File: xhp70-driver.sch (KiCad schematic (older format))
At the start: 13 parts

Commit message: Layout schematic, created AL8871Q symbol and footprint. Layout PCB.
Pending values for components and PCB traces.
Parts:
- C1, C2, C3: renamed from C?; footprint (none) -> Capacitor_SMD:C_1206_3216Metric_Pad1.33x1.80mm_HandSolder
- D1: renamed from D?; footprint (none) -> Diode_SMD:D_PowerDI-5
- D2: renamed from D?; footprint (none) -> Connector_Molex:Molex_Sabre_46007-1102_1x02_P7.49mm_Horizontal
- L1: renamed from L?; footprint (none) -> Inductor_SMD:L_12x12mm_H8mm
- Q1: renamed from Q?; footprint (none) -> Package_TO_SOT_SMD:TO-252-2
- R1, R2, R3, R4, R5: renamed from R?; footprint (none) -> Resistor_SMD:R_1206_3216Metric_Pad1.30x1.75mm_HandSolder
- U1: renamed from U?; footprint (none) -> xhp70-driver:AL8871Q
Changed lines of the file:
@@
 $EndDescr
 $Comp
-L LED-driver:AL8871Q U?
+L LED-driver:AL8871Q U1
 U 1 1 6031458B
 P 5300 3400
-F 0 "U?" H 6094 3471 50  0000 L CNN
+F 0 "U1" H 6094 3471 50  0000 L CNN
 F 1 "AL8871Q" H 6094 3380 50  0000 L CNN
-F 2 "" H 5250 4650 50  0001 C CNN
+F 2 "xhp70-driver:AL8871Q" H 5250 4650 50  0001 C CNN
 F 3 "" H 5250 4650 50  0001 C CNN
 	1    5300 3400
@@
 $EndComp
 $Comp
-L power:+BATT #PWR?
+L power:+BATT #PWR0101
 U 1 1 60315055
 P 2450 2200
-F 0 "#PWR?" H 2450 2050 50  0001 C CNN
+F 0 "#PWR0101" H 2450 2050 50  0001 C CNN
 F 1 "+BATT" H 2465 2373 50  0000 C CNN
 F 2 "" H 2450 2200 50  0001 C CNN
@@
 $EndComp
 $Comp
-L power:GND #PWR?
+L power:GND #PWR0102
 U 1 1 603158B1
 P 5500 5050
-F 0 "#PWR?" H 5500 4800 50  0001 C CNN
+F 0 "#PWR0102" H 5500 4800 50  0001 C CNN
 F 1 "GND" H 5505 4877 50  0000 C CNN
 F 2 "" H 5500 5050 50  0001 C CNN
@@
 $EndComp
 $Comp
-L Device:R R?
+L Device:R R1
 U 1 1 60317199
 P 2800 3950
-F 0 "R?" H 2870 3996 50  0000 L CNN
+F 0 "R1" H 2870 3996 50  0000 L CNN
 F 1 "R" H 2870 3905 50  0000 L CNN
-F 2 "" V 2730 3950 50  0001 C CNN
+F 2 "Resistor_SMD:R_1206_3216Metric_Pad1.30x1.75mm_HandSolder" V 2730 3950 50  0001 C CNN
 F 3 "~" H 2800 3950 50  0001 C CNN
 	1    2800 3950
@@
 $EndComp
 $Comp
-L Device:C C?
+L Device:C C1
 U 1 1 60318EA7
 P 2450 3100
-F 0 "C?" H 2565 3146 50  0000 L CNN
+F 0 "C1" H 2565 3146 50  0000 L CNN
 F 1 "C" H 2565 3055 50  0000 L CNN
-F 2 "" H 2488 2950 50  0001 C CNN
+F 2 "Capacitor_SMD:C_1206_3216Metric_Pad1.33x1.80mm_HandSolder" H 2488 2950 50  0001 C CNN
 F 3 "~" H 2450 3100 50  0001 C CNN
 	1    2450 3100
@@
 $EndComp
 $Comp
-L Device:R R?
+L Device:R R3
 U 1 1 6031A435
 P 3400 3950
-F 0 "R?" H 3470 3996 50  0000 L CNN
+F 0 "R3" H 3470 3996 50  0000 L CNN
 F 1 "R" H 3470 3905 50  0000 L CNN
-F 2 "" V 3330 3950 50  0001 C CNN
+F 2 "Resistor_SMD:R_1206_3216Metric_Pad1.30x1.75mm_HandSolder" V 3330 3950 50  0001 C CNN
 F 3 "~" H 3400 3950 50  0001 C CNN
 	1    3400 3950
@@
 $EndComp
 $Comp
-L Device:R R?
+L Device:R R4
 U 1 1 6031AA09
 P 3400 4500
-F 0 "R?" H 3470 4546 50  0000 L CNN
+F 0 "R4" H 3470 4546 50  0000 L CNN
 F 1 "R" H 3470 4455 50  0000 L CNN
-F 2 "" V 3330 4500 50  0001 C CNN
+F 2 "Resistor_SMD:R_1206_3216Metric_Pad1.30x1.75mm_HandSolder" V 3330 4500 50  0001 C CNN
 F 3 "~" H 3400 4500 50  0001 C CNN
 	1    3400 4500
@@
 $EndComp
 $Comp
-L Device:R R?
+L Device:R R2
 U 1 1 6031AE07
 P 2800 4500
-F 0 "R?" H 2870 4546 50  0000 L CNN
+F 0 "R2" H 2870 4546 50  0000 L CNN
 F 1 "R" H 2870 4455 50  0000 L CNN
-F 2 "" V 2730 4500 50  0001 C CNN
+F 2 "Resistor_SMD:R_1206_3216Metric_Pad1.30x1.75mm_HandSolder" V 2730 4500 50  0001 C CNN
 F 3 "~" H 2800 4500 50  0001 C CNN
 	1    2800 4500
@@
 $EndComp
 $Comp
-L Device:C C?
+L Device:C C2
 U 1 1 6031B075
 P 4350 4500
-F 0 "C?" H 4465 4546 50  0000 L CNN
+F 0 "C2" H 4465 4546 50  0000 L CNN
 F 1 "C" H 4465 4455 50  0000 L CNN
-F 2 "" H 4388 4350 50  0001 C CNN
+F 2 "Capacitor_SMD:C_1206_3216Metric_Pad1.33x1.80mm_HandSolder" H 4388 4350 50  0001 C CNN
 F 3 "~" H 4350 4500 50  0001 C CNN
 	1    4350 4500
@@
 $EndComp
 $Comp
-L Device:R R?
+L Device:R R5
 U 1 1 6031BBB3
 P 5500 2200
-F 0 "R?" V 5293 2200 50  0000 C CNN
+F 0 "R5" V 5293 2200 50  0000 C CNN
 F 1 "R" V 5384 2200 50  0000 C CNN
-F 2 "" V 5430 2200 50  0001 C CNN
+F 2 "Resistor_SMD:R_1206_3216Metric_Pad1.30x1.75mm_HandSolder" V 5430 2200 50  0001 C CNN
 F 3 "~" H 5500 2200 50  0001 C CNN
 	1    5500 2200
@@
 $EndComp
 $Comp
-L pspice:INDUCTOR L?
+L pspice:INDUCTOR L1
 U 1 1 6031C7F1
 P 7850 2750
-F 0 "L?" V 7804 2828 50  0000 L CNN
+F 0 "L1" V 7804 2828 50  0000 L CNN
 F 1 "INDUCTOR" V 7895 2828 50  0000 L CNN
-F 2 "" H 7850 2750 50  0001 C CNN
+F 2 "Inductor_SMD:L_12x12mm_H8mm" H 7850 2750 50  0001 C CNN
 F 3 "~" H 7850 2750 50  0001 C CNN
 	1    7850 2750
@@
 $EndComp
 $Comp
-L Device:Q_NMOS_GDS Q?
+L Device:Q_NMOS_GDS Q1
 U 1 1 603205DA
 P 7750 3350
-F 0 "Q?" H 7954 3396 50  0000 L CNN
+F 0 "Q1" H 7954 3396 50  0000 L CNN
 F 1 "Q_NMOS_GDS" H 7954 3305 50  0000 L CNN
-F 2 "" H 7950 3450 50  0001 C CNN
+F 2 "Package_TO_SOT_SMD:TO-252-2" H 7950 3450 50  0001 C CNN
 F 3 "~" H 7750 3350 50  0001 C CNN
 	1    7750 3350
@@
 $EndComp
 $Comp
-L Device:D D?
+L Device:D D1
 U 1 1 603221B3
 P 8700 3000
-F 0 "D?" H 8700 2783 50  0000 C CNN
+F 0 "D1" H 8700 2783 50  0000 C CNN
 F 1 "D" H 8700 2874 50  0000 C CNN
-F 2 "" H 8700 3000 50  0001 C CNN
+F 2 "Diode_SMD:D_PowerDI-5" H 8700 3000 50  0001 C CNN
 F 3 "~" H 8700 3000 50  0001 C CNN
 	1    8700 3000
@@
 $EndComp
 $Comp
-L Device:C C?
+L Device:C C3
 U 1 1 60322E55
 P 9000 2350
-F 0 "C?" H 9115 2396 50  0000 L CNN
+F 0 "C3" H 9115 2396 50  0000 L CNN
 F 1 "C" H 9115 2305 50  0000 L CNN
-F 2 "" H 9038 2200 50  0001 C CNN
+F 2 "Capacitor_SMD:C_1206_3216Metric_Pad1.33x1.80mm_HandSolder" H 9038 2200 50  0001 C CNN
 F 3 "~" H 9000 2350 50  0001 C CNN
 	1    9000 2350
@@
 $EndComp
 $Comp
-L Device:LED D?
+L Device:LED D2
 U 1 1 60323B1E
 P 9750 2350
-F 0 "D?" V 9697 2430 50  0000 L CNN
+F 0 "D2" V 9697 2430 50  0000 L CNN
 F 1 "LED" V 9788 2430 50  0000 L CNN
-F 2 "" H 9750 2350 50  0001 C CNN
+F 2 "Connector_Molex:Molex_Sabre_46007-1102_1x02_P7.49mm_Horizontal" H 9750 2350 50  0001 C CNN
 F 3 "~" H 9750 2350 50  0001 C CNN
 	1    9750 2350

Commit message: Added Attiny85 MCU to control PWM of AL8871Q
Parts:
- added H1, H2, H3, H4, H5: MountingHole, MountingHole:MountingHole_2.2mm_M2_ISO7380_Pad, symbol Mechanical:MountingHole
- added J1: LEMO2, xhp70-driver:TestPoint_2Pad_4.0x4.0mm, symbol Connector:LEMO2
- added J2: AVR-ISP-6, Connector_JST:JST_SH_BM06B-SRSS-TB_1x06-1MP_P1.00mm_Vertical, symbol Connector:AVR-ISP-6
- added J3: Conn_01x02_Male, Connector_JST:JST_SH_BM02B-SRSS-TB_1x02-1MP_P1.00mm_Vertical, symbol Connector:Conn_01x02_Male
- added TH1: 10K, xhp70-driver:TestPoint_2Pad_4.0x4.0mm, symbol Device:Thermistor_NTC
- added U2: ATtiny85-20SU, Package_SO:SOIJ-8_5.3x5.3mm_P1.27mm, symbol MCU_Microchip_ATtiny:ATtiny85-20SU
- added U3: L7805, Package_TO_SOT_SMD:SOT-23, symbol Regulator_Linear:L7805
- D2: footprint Connector_Molex:Molex_Sabre_46007-1102_1x02_P7.49mm_Horizontal -> xhp70-driver:TestPoint_2Pad_4.0x4.0mm
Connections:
- net labels added: Batt+, PWM
- wire segments 59 -> 93
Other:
- moved on the sheet: C1, C2, C3, D2, L1, Q1, R1, R2, R3, R5, U1

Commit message: Added components and route connections in xhp70-driver-test-route.pro file
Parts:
- removed D1: D, Diode_SMD:D_PowerDI-5, symbol Device:D
- removed R5: R, Resistor_SMD:R_1206_3216Metric_Pad1.30x1.75mm_HandSolder, symbol Device:R
- added C4: 1uF, Capacitor_SMD:C_1206_3216Metric_Pad1.33x1.80mm_HandSolder, symbol Device:C
- added C5: 100nF, Capacitor_SMD:C_0805_2012Metric, symbol Device:C
- added C6: 330pF, Capacitor_SMD:C_0805_2012Metric, symbol Device:C
- added D1: D_Schottky, xhp70-driver:TO-220-2_Horizontal_TabUp-no-mounting-hole, symbol Device:D_Schottky
- C1, C2: value C -> 10uF; Field4 (none) -> X7R, 100V
- C3: value C -> 1uF; Field4 (none) -> X7R, 100V, 1206
- J2: footprint Connector_JST:JST_SH_BM06B-SRSS-TB_1x06-1MP_P1.00mm_Vertical -> Connector_PinHeader_1.00mm:PinHeader_1x06_P1.00mm_Vertical
- Q1: footprint Package_TO_SOT_SMD:TO-252-2 -> xhp70-driver:TO-220-3_Horizontal_TabUp-no-mounting-hole
- R1: value R -> 0.09; footprint Resistor_SMD:R_1206_3216Metric_Pad1.30x1.75mm_HandSolder -> Resistor_SMD:R_2512_6332Metric; Field4 (none) -> 1W
- R2: value R -> 0.082; footprint Resistor_SMD:R_1206_3216Metric_Pad1.30x1.75mm_HandSolder -> Resistor_SMD:R_2512_6332Metric; Field4 (none) -> 1W
- R3: value R -> 2.2K; footprint Resistor_SMD:R_1206_3216Metric_Pad1.30x1.75mm_HandSolder -> Resistor_SMD:R_0805_2012Metric
- R4: value R -> 1.3K; footprint Resistor_SMD:R_1206_3216Metric_Pad1.30x1.75mm_HandSolder -> Resistor_SMD:R_0805_2012Metric
- R5: renamed from TH1; footprint xhp70-driver:TestPoint_2Pad_4.0x4.0mm -> Connector_JST:JST_SH_BM02B-SRSS-TB_1x02-1MP_P1.00mm_Vertical
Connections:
- wire segments 93 -> 92
- no-connect marks 2 -> 4
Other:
- moved on the sheet: C1, C3, D2, H1, H2, H4, H5, L1, Q1, R1, R2, R3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

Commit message: Reposition and changed connector. Reroute traces
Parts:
- J2: footprint Connector_PinHeader_1.00mm:PinHeader_1x06_P1.00mm_Vertical -> Connector_JST:JST_SH_BM06B-SRSS-TB_1x06-1MP_P1.00mm_Vertical
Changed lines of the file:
@@
 F 0 "J2" H 5370 6596 50  0000 R CNN
 F 1 "AVR-ISP-6" H 5370 6505 50  0000 R CNN
-F 2 "Connector_PinHeader_1.00mm:PinHeader_1x06_P1.00mm_Vertical" V 5450 6550 50  0001 C CNN
+F 2 "Connector_JST:JST_SH_BM06B-SRSS-TB_1x06-1MP_P1.00mm_Vertical" V 5450 6550 50  0001 C CNN
 F 3 " ~" H 4425 5950 50  0001 C CNN
 	1    5700 6500

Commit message: Updates
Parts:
- removed J3: Conn_01x02_Male, Connector_JST:JST_SH_BM02B-SRSS-TB_1x02-1MP_P1.00mm_Vertical, symbol Connector:Conn_01x02_Male
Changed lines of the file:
@@
 	4100 6450 4100 6550
-Wire Wire Line
-	4100 6550 4550 6550
-$Comp
-L Connector:Conn_01x02_Male J3
-U 1 1 603B34ED
-P 5200 7500
-F 0 "J3" H 5172 7382 50  0000 R CNN
-F 1 "Conn_01x02_Male" H 5172 7473 50  0000 R CNN
-F 2 "Connector_JST:JST_SH_BM02B-SRSS-TB_1x02-1MP_P1.00mm_Vertical" H 5200 7500 50  0001 C CNN
-F 3 "~" H 5200 7500 50  0001 C CNN
-	1    5200 7500
-	-1   0    0    1
-$EndComp
-Wire Wire Line
-	5000 7500 2150 7500
-Wire Wire Line
-	2150 7500 2150 5650
-Wire Wire Line
-	2100 5650 2150 5650
-Connection ~ 2150 5650
-Wire Wire Line
-	2150 5650 3250 5650
-Wire Wire Line
-	4550 6550 4550 7400
-Wire Wire Line
-	4550 7400 5000 7400
 Wire Wire Line
 	4300 6300 4300 6350
@@
 Wire Wire Line
 	5150 6500 5300 6500
-Connection ~ 4550 6550
-Wire Wire Line
-	4550 6550 5150 6550
 Wire Wire Line
 	4850 6250 4850 6400
@@
 Wire Wire Line
 	3450 1850 3900 1850
+Wire Wire Line
+	4100 6550 5150 6550
+Wire Wire Line
+	2100 5650 3250 5650
 $EndSCHEMATC

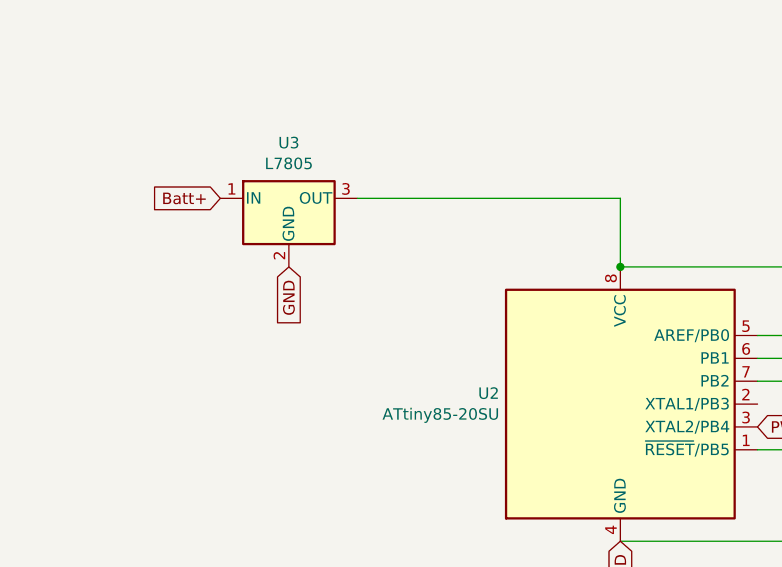
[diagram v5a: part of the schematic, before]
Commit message: LED driver rev.1b - Added decoupling Capacitors for Attiny
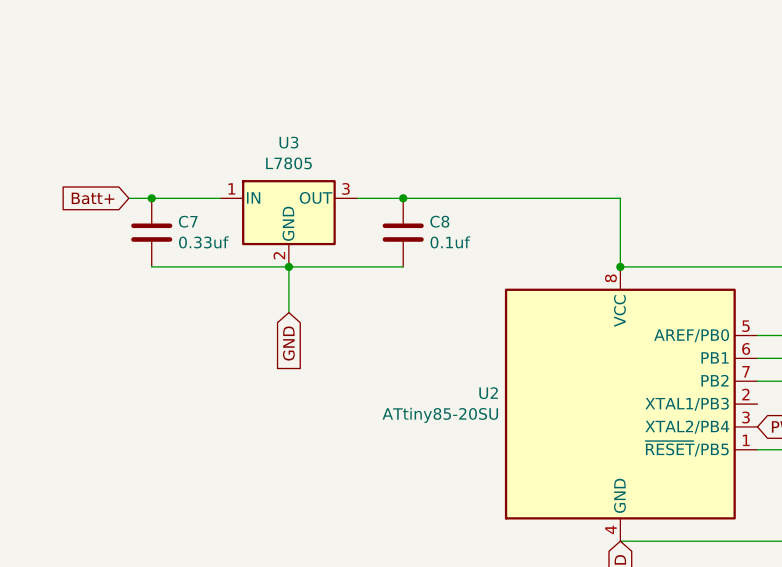
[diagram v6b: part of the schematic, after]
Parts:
- added C7: 0.33uf, Capacitor_SMD:C_0805_2012Metric, symbol Device:C
- added C8: 0.1uf, Capacitor_SMD:C_0805_2012Metric, symbol Device:C
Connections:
- net +BATT: now also C7.1
- net GND: now also C7.2, C8.2
- net at J2.2 (VCC), U2.8 (VCC), U3.3 (OUT): now also C8.1
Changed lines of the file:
@@
 Text GLabel 3850 6650 2    50   Input ~ 0
 PWM
-Text GLabel 1800 5950 3    50   Input ~ 0
+Text GLabel 1800 6150 3    50   Input ~ 0
 GND
 Text GLabel 3250 7150 3    50   Input ~ 0
 GND
-Text GLabel 1500 5650 0    50   Input ~ 0
+Text GLabel 1100 5650 0    50   Input ~ 0
 Batt+
 Wire Wire Line
@@
 	4100 6550 5150 6550
 Wire Wire Line
-	2100 5650 3250 5650
+	2100 5650 2300 5650
+$Comp
+L Device:C C7
+U 1 1 6043B427
+P 1200 5800
+F 0 "C7" H 1315 5846 50  0000 L CNN
+F 1 "0.33uf" H 1315 5755 50  0000 L CNN
+F 2 "Capacitor_SMD:C_0805_2012Metric" H 1238 5650 50  0001 C CNN
+F 3 "~" H 1200 5800 50  0001 C CNN
+	1    1200 5800
+	1    0    0    -1
+$EndComp
+$Comp
+L Device:C C8
+U 1 1 6043C0F6
+P 2300 5800
+F 0 "C8" H 2415 5846 50  0000 L CNN
+F 1 "0.1uf" H 2415 5755 50  0000 L CNN
+F 2 "Capacitor_SMD:C_0805_2012Metric" H 2338 5650 50  0001 C CNN
+F 3 "~" H 2300 5800 50  0001 C CNN
+	1    2300 5800
+	1    0    0    -1
+$EndComp
+Connection ~ 2300 5650
+Wire Wire Line
+	2300 5650 3250 5650
+Wire Wire Line
+	1800 6150 1800 5950
+Wire Wire Line
+	1800 5950 2300 5950
+Connection ~ 1800 5950
+Wire Wire Line
+	1200 5650 1500 5650
+Wire Wire Line
+	1100 5650 1200 5650
+Connection ~ 1200 5650
+Wire Wire Line
+	1200 5950 1800 5950
 $EndSCHEMATC
